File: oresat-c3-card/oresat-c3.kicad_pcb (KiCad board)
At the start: 4 copper layers, 99.8 x 94.6 mm, 504 parts, among them J1 TFM-120-01-L-D-RA, J3 2477330-1, J4 2477330-1, J5 DM3BT-DSF-PEJS, J6 Conn_01x02, J7 GRPB041VWVN-RC, J8 SM14B-SHLS-TF, Q1 DMP2035UQ-7, Q2 DMN3028LQ-7, Q3 DMP2035UQ-7, Q4 DMN3028LQ-7, Q6 MMBT2907, U1 OSD3358-1G-ISM, U10 SN74AUC1G07DCKR, U11 RCLAMP0504FB, U12 RCLAMP0504FB, U13 MAX892LEUA+T, U14 TLVH431, U16 AT86RF215, U17 SI4112-GM, U18 LT5534, U19 BDCN-20-13+, U20 QPC1022, U21 TQP7M9105, U22 LT5534, U23 NCS2-62+, U24 RV-3028-C7, U25 SN74LVC1G11IDCKRQ1, U26 TLV7041DBV, U27 SN74LVC1G04DCKR, U28 TLV1704-SEP, U29 TQP3M9036, U30 FM24CL64B-GTR, U31 LP2985AIM5-3.3, U34 TPS259621DDA, U35 TPS259620DDA, U36 LTC3624-5, U37 LTC4300A-1, U38 LP2985AIM5-3.3, U39 TCAN330, U4 BGB741L7ESD, U40 MAX941EUA+, U41 TQP3M9036, U42 74LVC2G34, U44 AT86RF215, U45 NCS2-62+, U47 QPC1022, U6 LTC3624-5, U7 MAC-24+, U8 TCAN330, U9 SFEM016GB1EA1TO-I-GE-121-STD, X1 TXETALSANF-26.000000, X3 TXETALSANF-26.000000, Y1 ECS-240-12-30BQ-AEN-TR, Y2 ABS07-32.768KHZ-T

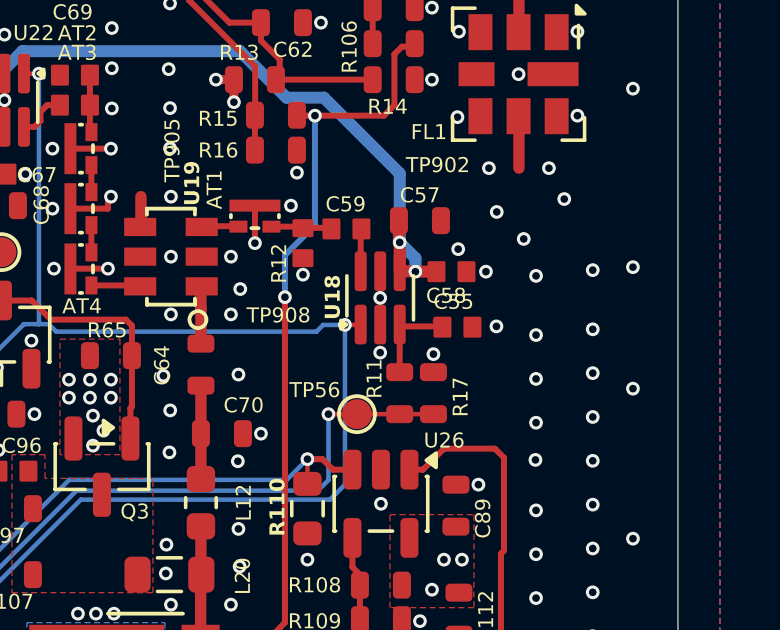
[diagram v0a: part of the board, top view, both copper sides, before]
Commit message: Fix BOM errors given feedback from CM
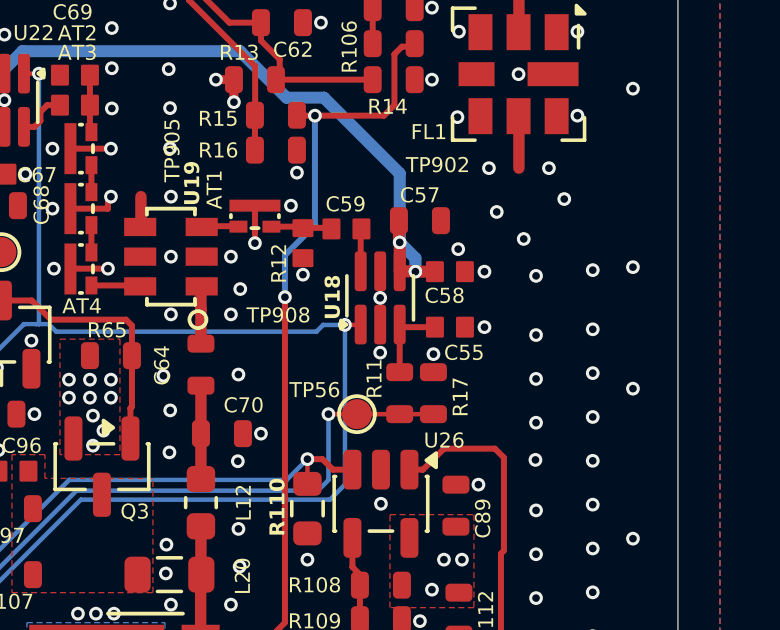
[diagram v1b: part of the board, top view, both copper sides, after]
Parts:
- X1, X3: value TXETALSANF-26.000000 -> TYETACSANF-26.000000
- moved C55 0.25 mm to (165.5, 73.0)
- moved C58 0.05 mm to (165.5, 71.1)
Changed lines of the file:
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@@
 	(footprint "oresat-passives:0402-B-NOSILK"
 		(layer "F.Cu")
-		(at 165.55 71.1)
+		(at 165.5 71.1)
 		(descr "<b>e0402 (metric 1005) normal 'IPC-B' without silkscreen</b>\n<br>In house package for nominal spacing based on IPC-7351B.\nThis package is identical to 0402-B, but has its tPlace silkscreen layer removed.")
 		(property "Reference" "C58"
@@
 			)
 		)
-		(property "MPN" "RMCF1206FT75R0"
+		(property "MPN" "RMCF0603FT75R0"
 			(at 0 0 90)
 			(unlocked yes)
@@
 			)
 		)
-		(property "Datasheet" "~"
+		(property "Datasheet" "https://content.kemet.com/datasheets/KEM_C1121_CBR_AUTO.pdf"
 			(at 0 0 90)
 			(layer "F.Fab")
@@
 			)
 		)
-		(property "Description" "18pF ±5% 50V Ceramic Capacitor C0G, NP0 0402 (1005 Metric)"
+		(property "Description" "18 pF ±5% 50V Ceramic Capacitor C0G, NP0 0402 (1005 Metric)"
 			(at 0 0 90)
 			(layer "F.Fab")
@@
 			)
 		)
-		(property "DPN" "399-15952-1-ND"
+		(property "DPN" "399-CBR04C180J5GACAUTOCT-ND"
 			(at 0 0 90)
 			(unlocked yes)
@@
 			)
 		)
-		(property "MPN" "C0402C180J5GACAUTO"
+		(property "MPN" "CBR04C180J5GACAUTO"
 			(at 0 0 90)
 			(unlocked yes)
@@
 			)
 		)
-		(property "MPN" "RMCF1206FT75R0"
+		(property "MPN" "RMCF0603FT75R0"
 			(at 0 0 90)
 			(unlocked yes)
@@
 			)
 		)
-		(property "Datasheet" "~"
+		(property "Datasheet" "https://content.kemet.com/datasheets/KEM_C1121_CBR_AUTO.pdf"
 			(at 0 0 90)
 			(layer "F.Fab")
@@
 			)
 		)
-		(property "Description" "18pF ±5% 50V Ceramic Capacitor C0G, NP0 0402 (1005 Metric)"
+		(property "Description" "18 pF ±5% 50V Ceramic Capacitor C0G, NP0 0402 (1005 Metric)"
 			(at 0 0 90)
 			(layer "F.Fab")
@@
 			)
 		)
-		(property "DPN" "399-15952-1-ND"
+		(property "DPN" "399-CBR04C180J5GACAUTOCT-ND"
 			(at 0 0 90)
 			(unlocked yes)
@@
 			)
 		)
-		(property "MPN" "C0402C180J5GACAUTO"
+		(property "MPN" "CBR04C180J5GACAUTO"
 			(at 0 0 90)
 			(unlocked yes)
@@
 			)
 		)
-		(property "Value" "TXETALSANF-26.000000"
+		(property "Value" "TYETACSANF-26.000000"
 			(at 0 -6.7 0)
 			(layer "F.Fab")
@@
 			)
 		)
-		(property "DPN" "1664-TXETALSANF-26.000000CT-ND"
+		(property "DPN" "1664-TYETACSANF-26.000000CT-ND"
 			(at 0 0 180)
 			(unlocked yes)
@@
 			)
 		)
-		(property "MPN" "TXETALSANF-26.000000"
+		(property "MPN" "TYETACSANF-26.000000"
 			(at 0 0 180)
 			(unlocked yes)
@@
 			)
 		)
-		(property "Datasheet" "https://yageogroup.com/content/datasheet/asset/file/KEM_C1022_C0G_AUTO_SMD"
+		(property "Datasheet" "https://content.kemet.com/datasheets/KEM_C1121_CBR_AUTO.pdf"
 			(at 0 0 180)
 			(layer "F.Fab")
@@
 			)
 		)
-		(property "Description" "22 pF ±5% 100V Ceramic Capacitor C0G, NP0 0603 (1608 Metric)"
+		(property "Description" "22 pF ±5% 50V Ceramic Capacitor C0G, NP0 0402 (1005 Metric)"
 			(at 0 0 180)
 			(layer "F.Fab")
@@
 			)
 		)
-		(property "DPN" "399-15987-1-ND"
+		(property "DPN" "399-CBR04C220J5GACAUTOCT-ND"
 			(at 0 0 180)
 			(unlocked yes)
@@
 			)
 		)
-		(property "MPN" "C0603C220J1GACAUTO"
+		(property "MPN" "CBR04C220J5GACAUTO"
 			(at 0 0 180)
 			(unlocked yes)
@@
 			)
 		)
-		(property "Datasheet" "https://yageogroup.com/content/datasheet/asset/file/KEM_C1022_C0G_AUTO_SMD"
+		(property "Datasheet" "https://content.kemet.com/datasheets/KEM_C1121_CBR_AUTO.pdf"
 			(at 0 0 270)
 			(layer "F.Fab")
@@
 			)
 		)
-		(property "Description" "22 pF ±5% 100V Ceramic Capacitor C0G, NP0 0603 (1608 Metric)"
+		(property "Description" "22 pF ±5% 50V Ceramic Capacitor C0G, NP0 0402 (1005 Metric)"
 			(at 0 0 270)
 			(layer "F.Fab")
@@
 			)
 		)
-		(property "DPN" "399-15987-1-ND"
+		(property "DPN" "399-CBR04C220J5GACAUTOCT-ND"
 			(at 0 0 270)
 			(unlocked yes)
@@
 			)
 		)
-		(property "MPN" "C0603C220J1GACAUTO"
+		(property "MPN" "CBR04C220J5GACAUTO"
 			(at 0 0 270)
 			(unlocked yes)
@@
 			)
 		)
-		(property "Datasheet" "https://yageogroup.com/content/datasheet/asset/file/KEM_C1022_C0G_AUTO_SMD"
+		(property "Datasheet" "https://content.kemet.com/datasheets/KEM_C1121_CBR_AUTO.pdf"
 			(at 0 0 180)
 			(layer "F.Fab")
@@
 			)
 		)
-		(property "Description" "22 pF ±5% 100V Ceramic Capacitor C0G, NP0 0603 (1608 Metric)"
+		(property "Description" "22 pF ±5% 50V Ceramic Capacitor C0G, NP0 0402 (1005 Metric)"
 			(at 0 0 180)
 			(layer "F.Fab")
@@
 			)
 		)
-		(property "DPN" "399-15987-1-ND"
+		(property "DPN" "399-CBR04C220J5GACAUTOCT-ND"
 			(at 0 0 180)
 			(unlocked yes)
@@
 			)
 		)
-		(property "MPN" "C0603C220J1GACAUTO"
+		(property "MPN" "CBR04C220J5GACAUTO"
 			(at 0 0 180)
 			(unlocked yes)
@@
 			)
 		)
-		(property "Value" "TXETALSANF-26.000000"
+		(property "Value" "TYETACSANF-26.000000"
 			(at 0 -6.7 0)
 			(layer "F.Fab")
@@
 			)
 		)
-		(property "DPN" "1664-TXETALSANF-26.000000CT-ND"
+		(property "DPN" "1664-TYETACSANF-26.000000CT-ND"
 			(at 0 0 180)
 			(unlocked yes)
@@
 			)
 		)
-		(property "MPN" "TXETALSANF-26.000000"
+		(property "MPN" "TYETACSANF-26.000000"
 			(at 0 0 180)
 			(unlocked yes)
@@
 	(footprint "oresat-passives:0402-B-NOSILK"
 		(layer "F.Cu")
-		(at 165.75 72.95)
+		(at 165.5 72.95)
 		(descr "<b>e0402 (metric 1005) normal 'IPC-B' without silkscreen</b>\n<br>In house package for nominal spacing based on IPC-7351B.\nThis package is identical to 0402-B, but has its tPlace silkscreen layer removed.")
 		(property "Reference" "C55"
-			(at -0.8 -0.55 0)
+			(at -0.2 1.15 0)
 			(layer "F.SilkS")
 			(effects
@@
 	)
 	(segment
-		(start 163.825 72.925)
-		(end 165.025 72.925)
+		(start 165.025 72.75)
+		(end 165.05 72.775)
 		(width 0.2)
 		(layer "F.Cu")
@@
 	)
 	(segment
-		(start 165.025 72.75)
-		(end 165.05 72.775)
+		(start 163.825 74.45)
+		(end 163.825 72.75)
 		(width 0.2)
 		(layer "F.Cu")
@@
 	)
 	(segment
-		(start 163.825 74.45)
-		(end 163.825 72.75)
+		(start 165 72.95)
+		(end 165.025 72.925)
 		(width 0.2)
 		(layer "F.Cu")
@@
 	(segment
 		(start 163.85 72.95)
-		(end 163.825 72.925)
+		(end 165 72.95)
 		(width 0.2)
 		(layer "F.Cu")
@@
 	)
 	(segment
+		(start 164.35 71.1)
+		(end 165 71.1)
+		(width 0.4)
+		(layer "F.Cu")
+		(net 112)
+	)
+	(segment
 		(start 161.25 109.05)
 		(end 160.225 109.05)
@@
 	)
 	(segment
-		(start 164.35 71.1)
-		(end 165.05 71.1)
-		(width 0.4)
-		(layer "F.Cu")
-		(net 112)
-	)
-	(segment
 		(start 163.8 70.1)
 		(end 163.825 70.125)
@@
 	)
 	(via
-		(at 167.05 72.925)
+		(at 166.65 72.95)
 		(size 0.4572)
 		(drill 0.254)
@@
 	)
 	(via
-		(at 166.7 71.1)
+		(at 166.65 71.1)
 		(size 0.4572)
 		(drill 0.254)
